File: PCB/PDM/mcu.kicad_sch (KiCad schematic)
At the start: 34 parts, among them IC1 STM32L496ZGT6, IC2 AT25SF128A-SHB-T, Y1 48Mhz, Y2 32KHz

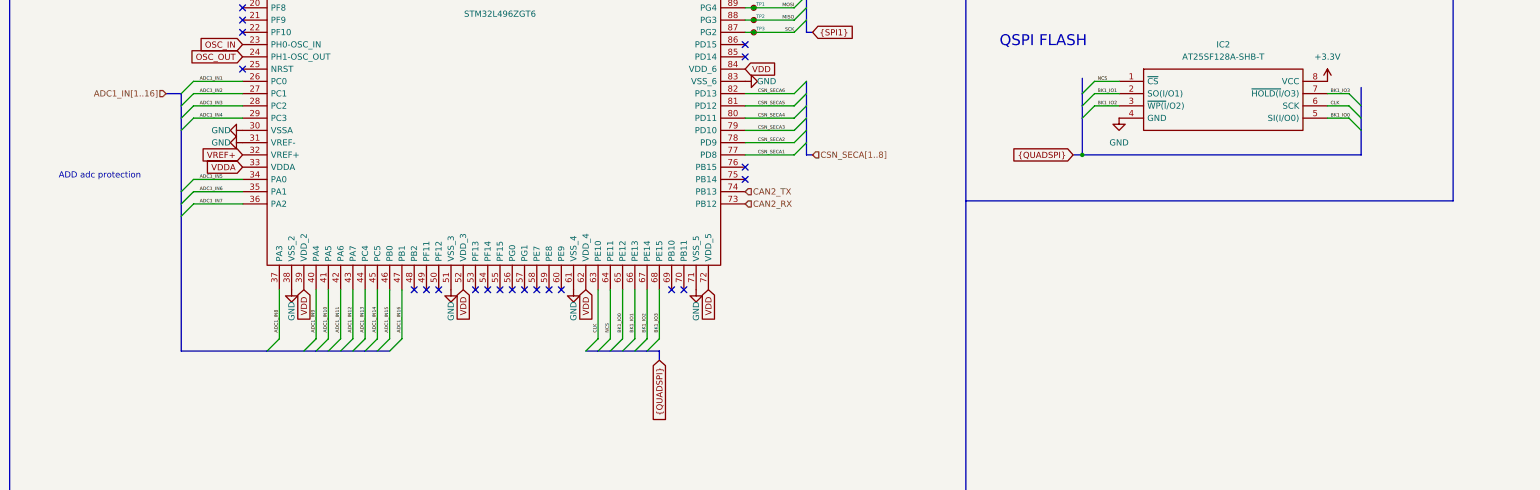
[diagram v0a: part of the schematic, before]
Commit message: Added adc protection and HC header radsock
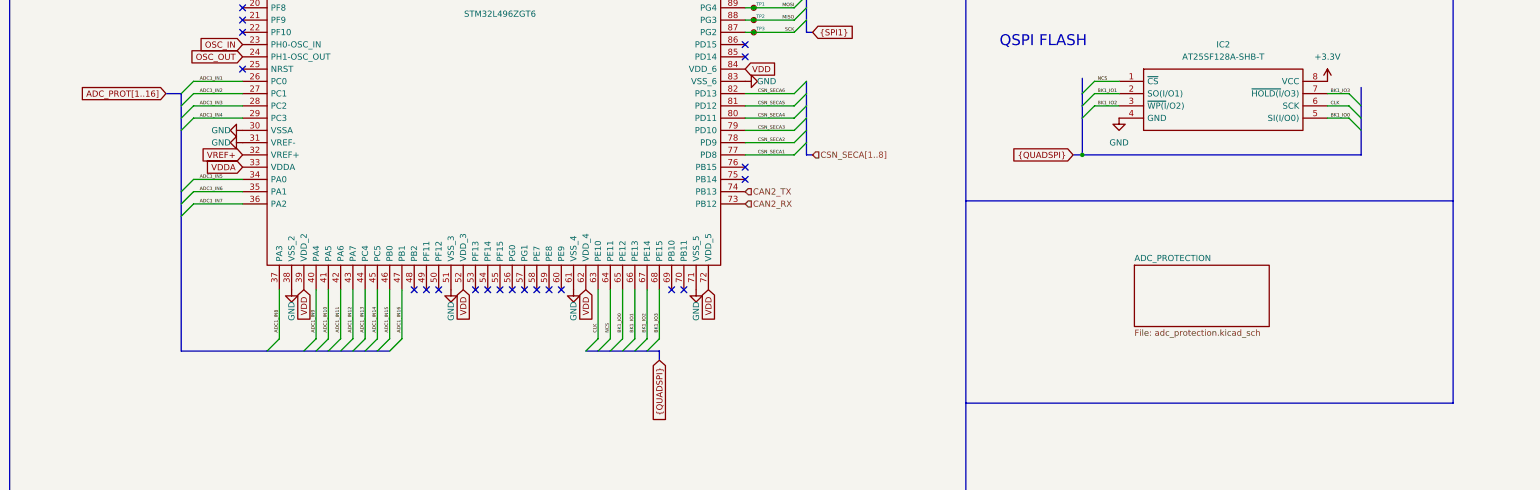
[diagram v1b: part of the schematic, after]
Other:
- added sheet ADC_PROTECTION (adc_protection.kicad_sch)
- note removed: "ADD adc protection"
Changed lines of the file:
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@@
   (paper "A3")
   (bus_alias "QUADSPI" (members "CLK" "NCS" "BK1_IO0" "BK1_IO1" "BK1_IO2" "BK1_IO3"))
+  (bus_alias "SPI1" (members "SCK" "MISO" "MOSI"))
   (bus_alias "SPI3" (members "SCK" "MISO" "MOSI"))
   (bus_alias "SPI2" (members "SCK" "MISO" "MOSI"))
-  (bus_alias "SPI1" (members "SCK" "MISO" "MOSI"))
   (junction (at 279.4 109.22) (diameter 0) (color 0 0 0 0)
   )
@@
     (stroke (width 0) (type default) (color 0 0 0 0))
   )
+  (polyline (pts (xy 209.55 235.585) (xy 310.515 235.585))
+    (stroke (width 0) (type default) (color 0 0 0 0))
+  )
   (wire (pts (xy 284.48 50.8) (xy 283.21 50.8))
     (stroke (width 0) (type default) (color 0 0 0 0))
@@
   )
   (bus (pts (xy 291.465 176.53) (xy 291.465 179.07))
+    (stroke (width 0) (type default) (color 0 0 0 0))
+  )
+  (polyline (pts (xy 310.515 235.585) (xy 310.515 193.675))
     (stroke (width 0) (type default) (color 0 0 0 0))
   )
@@
   (text "LSE" (at 267.97 22.225 0)
     (effects (font (size 2.2606 2.2606)) (justify left bottom))
-  )
-  (text "ADD adc protection" (at 21.59 189.23 0)
-    (effects (font (size 1.27 1.27)) (justify left bottom))
   )
   (text "Use high-quality ceramic capacitors designed for high-frequency (5-20pF)."
@@
     )
   )
+  (global_label "ADC_PROT[1..16]" (shape input) (at 43.815 171.45 180) (fields_autoplaced)
+    (effects (font (size 1.27 1.27)) (justify right))
+    (property "Intersheet References" "${INTERSHEET_REFS}" (id 0) (at 25.4362 171.3706 0)
+      (effects (font (size 1.27 1.27)) (justify right) hide)
+    )
+  )
   (global_label "VDDA" (shape input) (at 285.115 132.08 0) (fields_autoplaced)
     (effects (font (size 1.27 1.27)) (justify left))
@@
   (hierarchical_label "SWCLK" (shape input) (at 156.21 82.55 90)
     (effects (font (size 1.27 1.27)) (justify left))
-  )
-  (hierarchical_label "ADC1_IN[1..16]" (shape input) (at 43.815 171.45 180)
-    (effects (font (size 1.27 1.27)) (justify right))
   )
   (hierarchical_label "CSN_SECA[1..8]" (shape input) (at 177.8 184.15 0)
@@
     (pin "2")
   )
+  (sheet (at 244.475 207.01) (size 27.94 12.7) (fields_autoplaced)
+    (stroke (width 0.1524) (type solid) (color 0 0 0 0))
+    (fill (color 0 0 0 0.0000))
+    (property "Sheet name" "ADC_PROTECTION" (id 0) (at 244.475 206.2984 0)
+      (effects (font (size 1.27 1.27)) (justify left bottom))
+    )
+    (property "Sheet file" "adc_protection.kicad_sch" (id 1) (at 244.475 220.2946 0)
+      (effects (font (size 1.27 1.27)) (justify left top))
+    )
+  )
 )
